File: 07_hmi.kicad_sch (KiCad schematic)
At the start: 10 parts, among them SW1 Omron B3U-1000P, SW2 Omron B3U-1000P, SW3 Omron B3U-1000P, SW4 Omron B3U-1000P

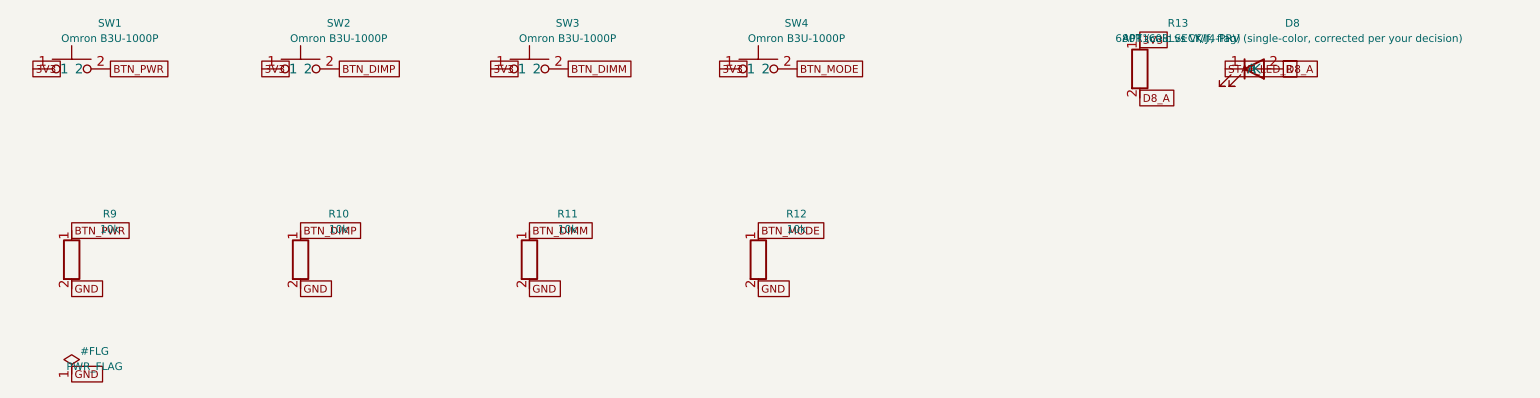
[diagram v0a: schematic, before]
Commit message: Root sheet + full-hierarchy fixes (PWR_FLAG uniqueness, annotation, D-designator collision)
- red-light-panel.kicad_sch: 7 sheet symbols, no sheet-pins (global-label
  connectivity throughout, see docs/design_notes.md).
- tools/kicad_gen/fix_instance_paths.py: one-time pass populating each
  sub-sheet's per-symbol instances block with the real root-relative path
  (kicad-cli sch upgrade was silently emptying these -- invisible to ERC,
  but kicad-cli sch export bom flagged it as an annotation error).
- Fixed: multiple PWR_FLAGs on the same merged net conflicting with each
  other at full-hierarchy scale (now exactly one per net, project-wide);
  duplicate unnumbered '#FLG' references across sheets; a real
  reference-designator collision in the original BOM itself (D5-D68 LED
  range numerically includes D6/D7/D8, reused for sheet 6/7 parts --
  renumbered those three to D69/D70/D71).

Full-hierarchy 'kicad-cli sch erc' on the root sheet: 0 errors (157
cosmetic endpoint-off-grid warnings, 3 expected lib_symbol_mismatch
warnings from flattened extends-based parts). 'kicad-cli sch export bom':
153 rows, zero blank footprints, zero duplicate references, no
annotation warning.

Co-Authored-By: Claude Sonnet 5 <noreply@anthropic.com>
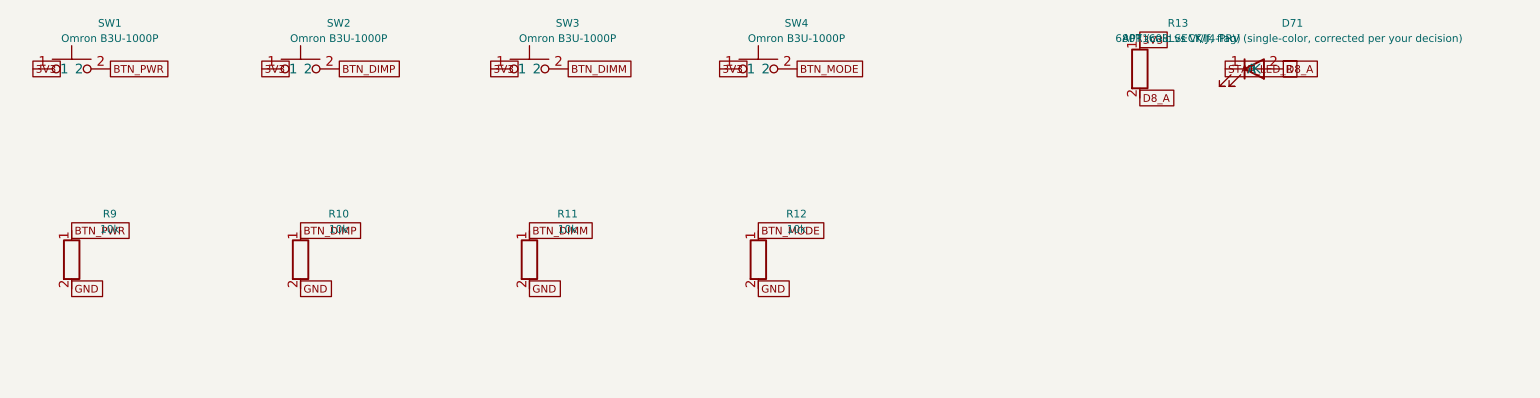
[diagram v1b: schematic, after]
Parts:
- removed D8: APT1608LSECK/J4-PRV (single-color, corrected per 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, LED_SMD:LED_0603_1608Metric, symbol Device:LED
- added D71: APT1608LSECK/J4-PRV (single-color, corrected per 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, LED_SMD:LED_0603_1608Metric, symbol Device:LED
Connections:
- net D8_A: now also D71.2 (A)
- net STAT_LED_R: now also D71.1 (K)

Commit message: Schematic: replace global-label power nets with real power symbols
GND, VBAT, VBAT_PROT, 3V3, and USB_VBUS now get an actual KiCad power
symbol at every pin (power:GND, power:+3V3 with Value overridden to
'3V3', power:VBUS overridden to 'USB_VBUS', and two custom symbols for
VBAT/VBAT_PROT copied from stock power:+BATT into
libs/red-light-panel.kicad_sym) instead of a plain GlobalLabel -- the
idiomatic convention for power rails. All other cross-sheet signal nets
(I2C, PWM, LED channel outputs, etc.) remain GlobalLabels, which still
makes sense for data/PWM signals.

Confirmed empirically before rolling this out: overriding a stock power
symbol's Value does change its effective net name (power:+3V3 with
Value='3V3' correctly nets as '3V3'), and every power symbol's pin is
still power_in (never power_out), so existing PWR_FLAG placements are
unaffected. 0 ERC errors after the change; BOM still 153 components /
48 grouped rows, zero blank footprints, zero duplicate references.

Co-Authored-By: Claude Sonnet 5 <noreply@anthropic.com>
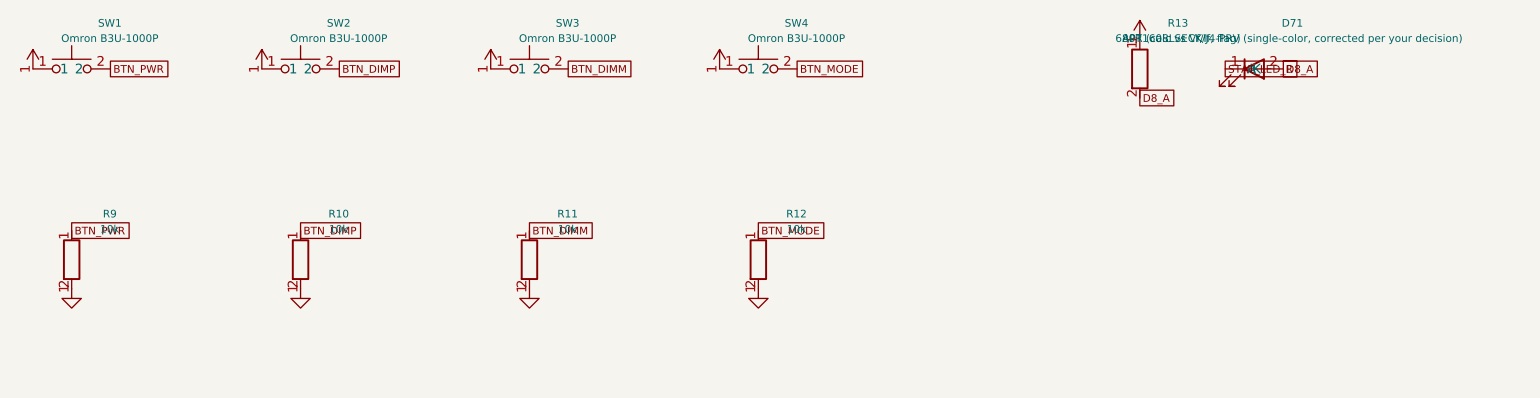
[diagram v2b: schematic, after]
